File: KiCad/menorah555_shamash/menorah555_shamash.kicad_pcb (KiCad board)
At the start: 2 copper layers, 17.6 x 79.8 mm, 8 parts, among them J3 Plug5.5x2.1

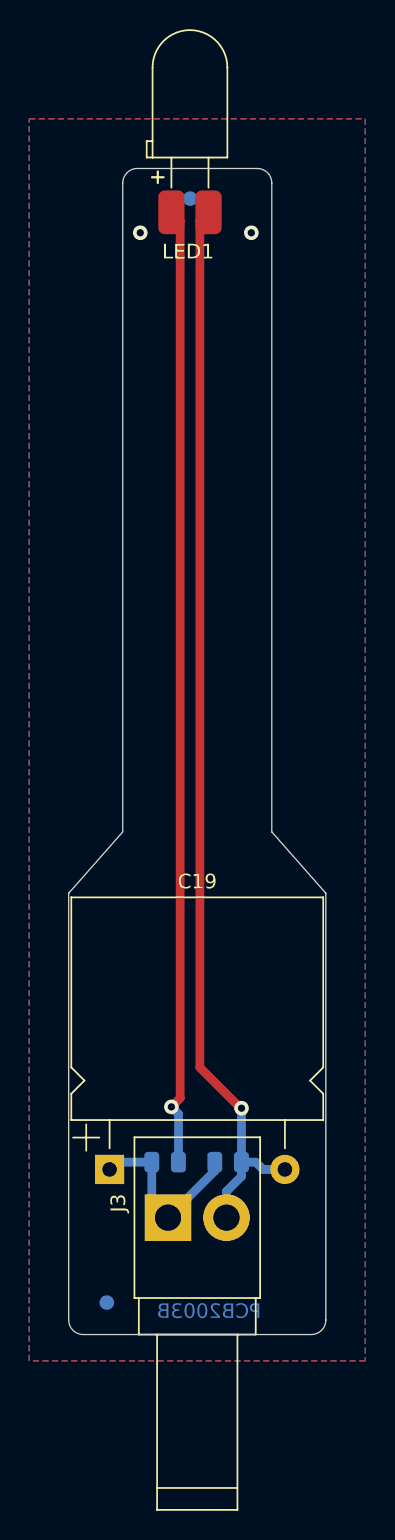
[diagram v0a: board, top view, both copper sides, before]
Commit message: Eliminated silkscreen crossing edge cuts
The DRC was giving warnings for silkscreen that overlapped with edge
cuts because it was getting cut by the soldermask. The footprints for
the LEDs and the shamash power connector were updated to delete the
silkscreen outside of the board edge cuts
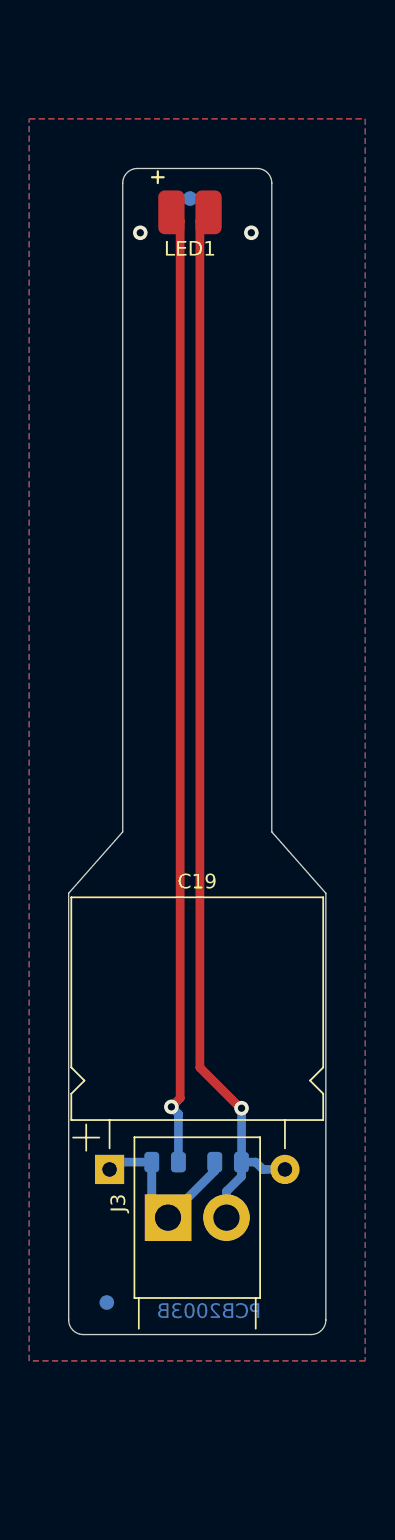
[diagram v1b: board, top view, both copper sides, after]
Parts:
- LED1: footprint 0_my_footprints:LED_D5.0mm_Horizontal_SMT_O3.81mm_Z3.0mm -> 0_project_footprints:LED_D5.0mm_Horizontal_SMT_O3.81mm
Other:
- outline, holes or cut-outs redrawn

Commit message: Added silkscreen 2mm stripe at edge
For aesthetic reasons, a 2mm silkscreen strip was added around the board
on top and bottom. Gerbers were also generated
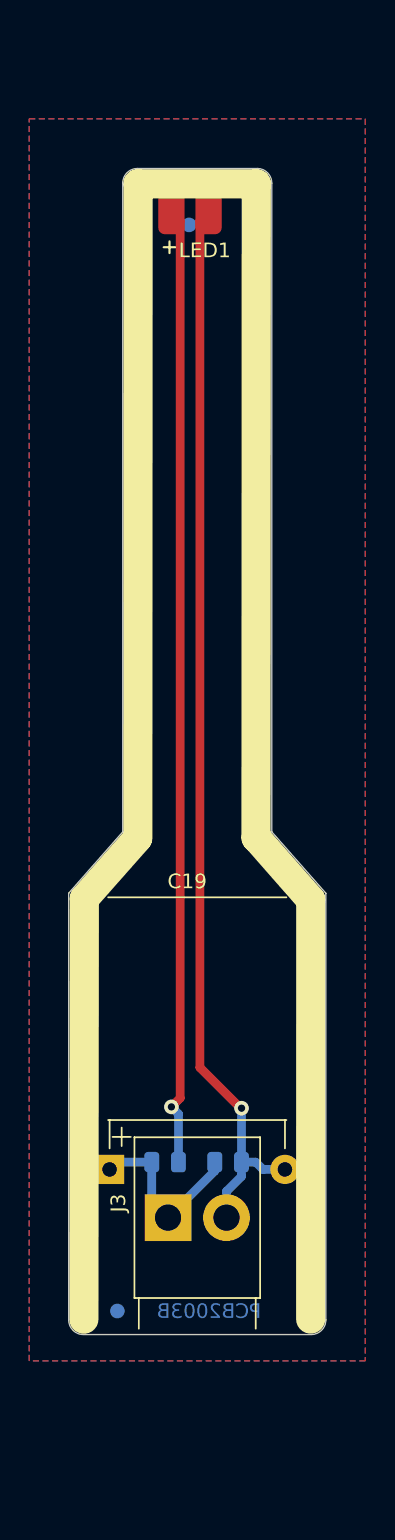
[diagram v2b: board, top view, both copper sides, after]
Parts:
- C19: footprint 0_my_footprints:CP_Supercap_DGH504Q5R5_Horizontal -> 0_project_footprints:CP_Supercap_DGH504Q5R5_Horizontal_narrow
- moved LOGO2 3.84 mm to (114.3, 123.0)
- moved FID3 1.80 mm to (113.6, 68.7)
- moved FID4 0.92 mm to (108.7, 143.0)
